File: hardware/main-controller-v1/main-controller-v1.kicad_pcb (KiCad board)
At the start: 2 copper layers, 162.7 x 112.7 mm, 62 parts, among them J1 B6B-PH-K-S, J2 Screw_Terminal_01x02, J3 Screw_Terminal_01x02, J4 Screw_Terminal_01x02, J6 Screw_Terminal_01x14, K1 G3MB-202P, K10 G3MB-202P, K11 G3MB-202P, K12 G3MB-202P, K2 G3MB-202P, K3 G3MB-202P, K4 G3MB-202P, K5 G3MB-202P, K6 G3MB-202P, K7 G3MB-202P, K8 G3MB-202P, K9 G3MB-202P, SW1 SW_Push, SW2 SW_Push, U1 ESP32-S3-WROOM-1, U2 USBLC6-2SC6, U3 LM2596S-5, U4 AP2112K-3.3

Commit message: fix(hardware): replace D2 bridge rectifier with MB10S, add bring-up jumpers, C7 footprint fix
- D2: DB107S (C5377, Extended) → MB10S (C2488, Basic); symbol+footprint
  imported via easyeda2kicad, DFM-authoritative pinout resolves the D2
  pad-swap risk that killed rev1 confidence
- Add R_JMP1-4 (0Ω 1206) on 24VAC_HOT, +VRAW, +5V, +3V3 for per-rail
  current measurement during bring-up
- C7 footprint: CP_Elec_6.3x5.4 → CP_Elec_5x5.8 (matches purchased part)
- Regenerate production/ gerbers, BOM, and CPL to match
- Track Azul.kicad_sym + Azul.pretty/MBS_* + Azul.3dshapes/ + sym-lib-table
  so the schematic resolves on a fresh clone
- Save datasheets for rev2 triac stage (MOC3062M, BT137-600E) and the
  G3MB-202P EOL catalog from Yuke Chip
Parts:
- added R_JMP1: 0, Resistor_SMD:R_1206_3216Metric, F.Cu at (106.5, 89.5)
- added R_JMP2: 0, Resistor_SMD:R_1206_3216Metric, F.Cu at (120.5, 104.0)
- added R_JMP3: 0, Resistor_SMD:R_1206_3216Metric, F.Cu at (78.5, 100.5)
- added R_JMP4: 0, Resistor_SMD:R_1206_3216Metric, F.Cu at (96.5, 72.5)
- C7: footprint Capacitor_SMD:CP_Elec_6.3x5.4 -> Capacitor_SMD:CP_Elec_5x5.8
- D2: value DB107S -> MB10S_C2488; footprint Diode_SMD:Diode_Bridge_Diotec_SO-DIL-Slim -> Azul:MBS_L4.7-W3.8-P2.40-LS7.0-TL
- moved C7 23.0 mm to (96.3, 109.0)
- moved C5 21.9 mm to (112.0, 105.5)
- moved D2 10.9 mm to (96.5, 97.5), turned to 180 degrees
- moved C6 6.85 mm to (122.5, 111.0)
- moved D1 1.00 mm to (103.5, 108.4)
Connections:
- C10 pad 1: +3V3 -> Net-(U4-VOUT)
- C6 pad 1: /+VRAW -> Net-(U3-VIN)
- C7 pad 1: +5V -> Net-(U3-FB)
- C9 pad 2: +3V3 -> Net-(U4-VOUT)
- D2 pad 1: 24VAC_HOT -> /+VRAW
- D2 pad 4: /+VRAW -> 24VAC_HOT
- F1 pad 2: Net-(J2-Pin_1) -> Net-(F1-Pad2)
- J1 pad 2: GND -> /USB_D-_RAW
- J1 pad 4: /USB_D-_RAW -> Net-(J1-Pin_4)
- J1 pad 6: Net-(J1-Pin_6) -> GND
- L1 pad 2: +5V -> Net-(U3-FB)
- R3 pad 1: Net-(J1-Pin_5) -> Net-(J1-Pin_4)
- R4 pad 1: Net-(J1-Pin_6) -> Net-(J1-Pin_5)
- U3 pad 1: /+VRAW -> Net-(U3-VIN)
- U3 pad 4: +5V -> Net-(U3-FB)
- U4 pad 5: +3V3 -> Net-(U4-VOUT)
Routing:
- net +5V: track 221.0 -> 163.9 mm, vias 4 -> 2
- net Net-(U3-FB): track 0.00 -> 47.7 mm
- net Net-(U3-VIN): track 0.00 -> 23.0 mm
- net /+VRAW: track 40.1 -> 25.6 mm
- net Net-(U4-VOUT): track 0.00 -> 11.2 mm
- net Net-(J1-Pin_6): track 9.56 -> 0.00 mm
- net Net-(J1-Pin_4): track 0.00 -> 8.97 mm
- net Net-(F1-Pad2): track 0.00 -> 5.59 mm
- net 24VAC_HOT: track 190.1 -> 185.9 mm
- net /USB_D-_RAW: track 22.6 -> 26.4 mm
- net 24VAC_COM: track 111.6 -> 110.3 mm, vias 1 -> 0
- net Net-(J2-Pin_1): track 8.59 -> 9.49 mm
- net GND: track 0.85 -> 0.00 mm, vias 49 -> 48
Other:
- board text removed: "Bridge Rectifier"

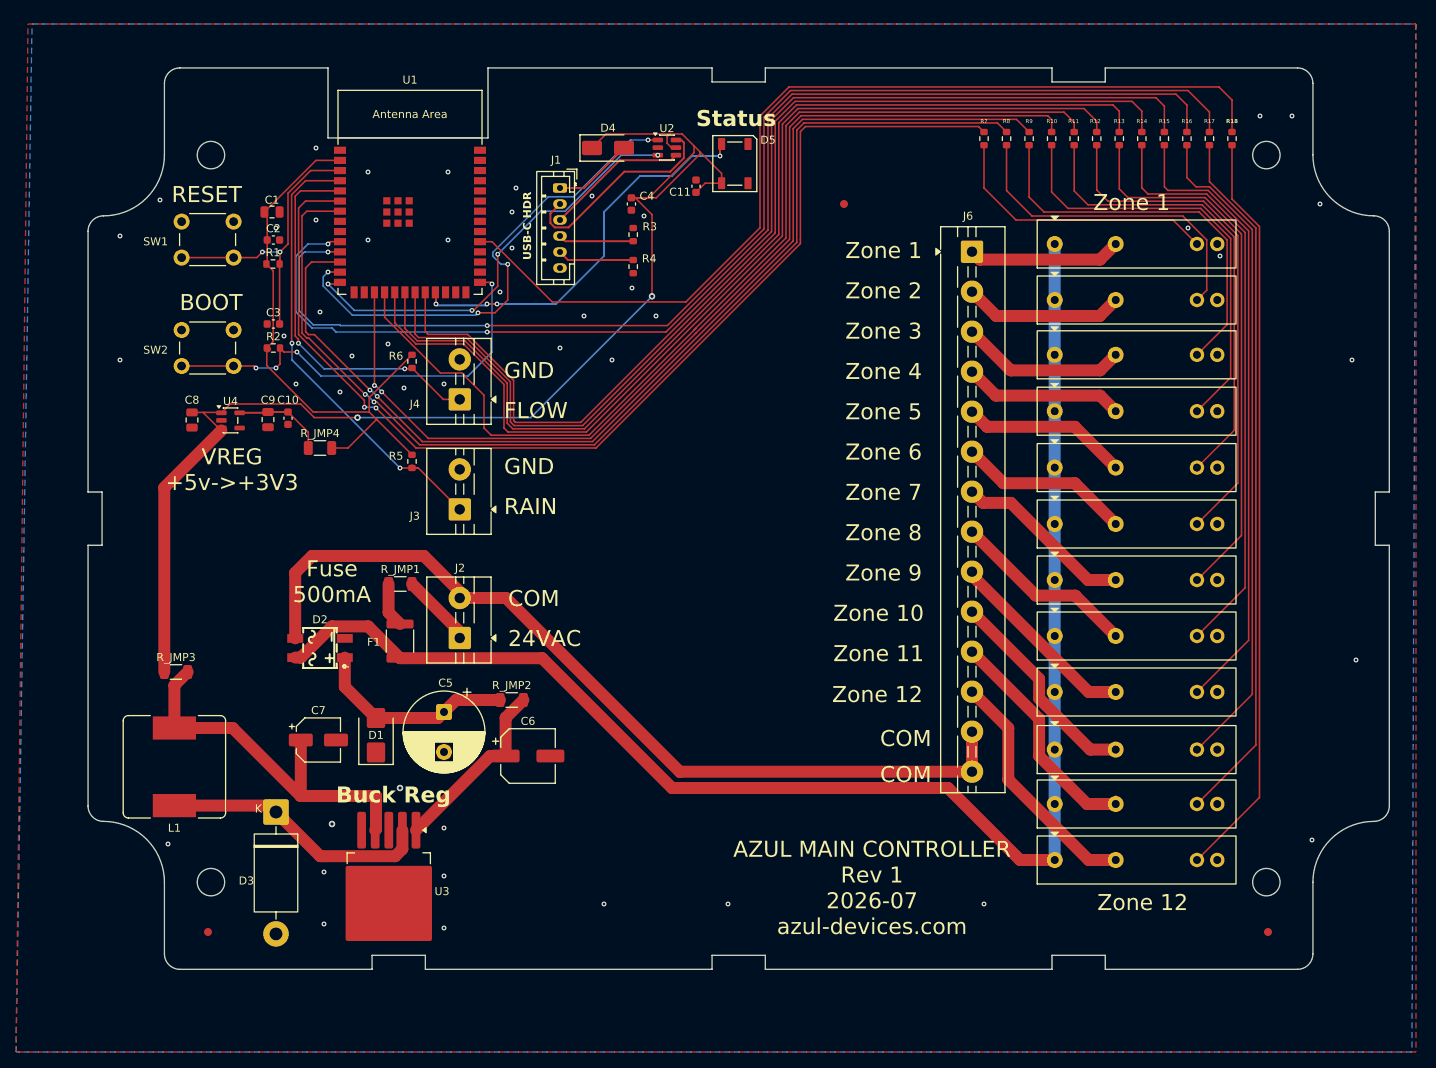
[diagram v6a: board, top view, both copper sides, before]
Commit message: feat(hardware): rev2 fab package — 12× discrete triac zone drivers
Rev2 replaces the EOL Omron G3MB-202P SSRs with a discrete triac zone-
driver topology (MOC3062M opto-isolated zero-cross trigger → BT137-600E
triac, per-zone snubber and X2 line cap). Twelve identical zone-driver
hierarchical sheets fan out from the parent under a single ribbon
header, driven active-high from the WROOM GPIOs.

Fab package uploaded to JLC 2026-08-08 as order W2026080821415396
(5 boards, Standard PCBA, UPS Express DDP, ~2026-08-18 delivery).

Design changes
- Delete K1–K12 G3MB relays; instantiate zone-driver.kicad_sch × 12
- Renumber R/C/U/Q across all 12 zone sheets (Q1–Q12 triacs,
  U5–U16 opto-drivers, C12–C23 X2 caps, R7–R42 zone stage)
- parts.yaml rev2 BOM: BT137-600E C967624, MOC3062M C8919,
  10nF X2 C105755, 39Ω 2010 snubber C2692665
- New Azul.pretty footprints + 3D models for DIP-6 opto, TO-220
  triac, and CAP-TH X2 (10mm pitch)
- Silkscreen title block "Rev 2 · 2026-08"

Fab workflow tooling
- scripts/apply_lcsc_fields.py: patches .kicad_sch LCSC fields from
  parts.yaml (BOM source of truth)
- jlc-dnp-lookup.md: fate: dnp vs smt decision matrix per part
- JLC_UPLOAD_TRACKER.md: 5-step walkthrough incorporating rev1
  lessons (J1 orientation, D2 pad-swap, CPL rotation offsets)
- Fixed DNP-flag sync bug — direct .kicad_pcb (attr) edit to strip
  stale dnp from J2/J3/J4 after fate: dnp→smt flip

Datasheets committed under docs/hardware/ for all rev2-new Extended
parts (C105755 X2, C2692665 39Ω 2010, C5188434 MX126 terminal,
C3817964, C6947975).

.gitignore: filter kicad-cli export intermediates (*.pre-*-backup,
DRC-output.rpt, update-pcb-report.txt) and the docs/azul v1 - Omega/
reference dump.
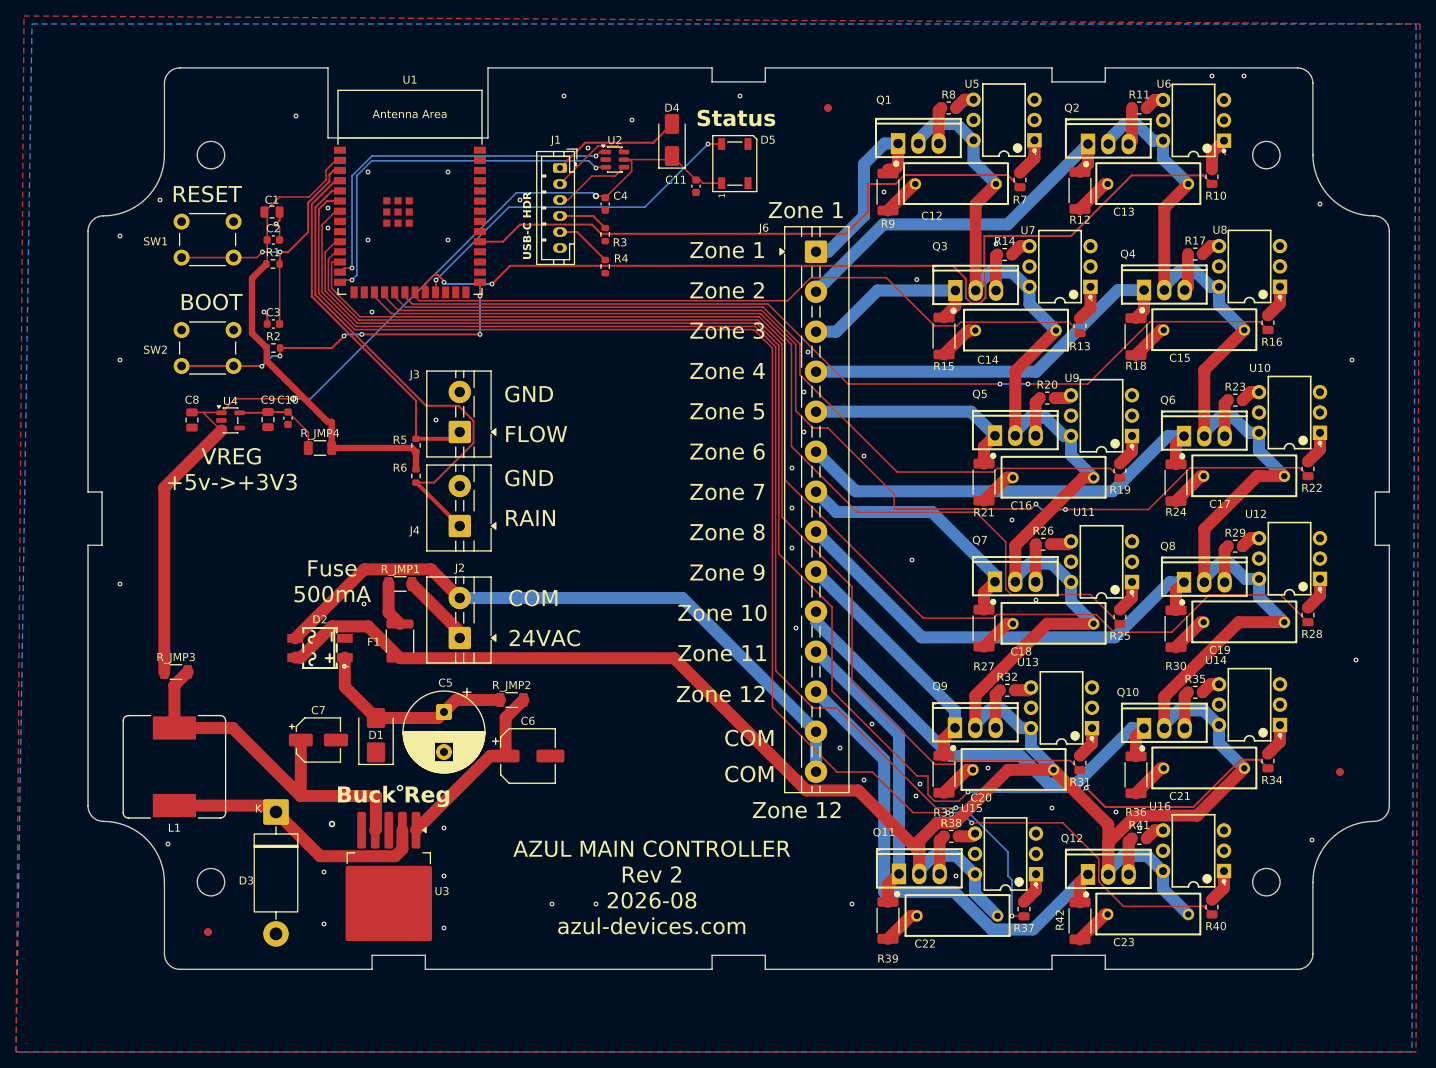
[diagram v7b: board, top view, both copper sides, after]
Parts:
- removed K1, K10, K11, K12, K2, K3, K4, K5, K6, K7, K8, K9: G3MB-202P, Azul:G3MB-202P
- added C12: 10nF, Azul:CAP-TH_L13.0-W5.0-P10.00-D1.0, F.Cu at (176.0, 39.5)
- added C13: 10nF, Azul:CAP-TH_L13.0-W5.0-P10.00-D1.0, F.Cu at (200.0, 39.5)
- added C14: 10nF, Azul:CAP-TH_L13.0-W5.0-P10.00-D1.0, F.Cu at (183.5, 57.8)
- added C15: 10nF, Azul:CAP-TH_L13.0-W5.0-P10.00-D1.0, F.Cu at (207.0, 57.8)
- added C16: 10nF, Azul:CAP-TH_L13.0-W5.0-P10.00-D1.0, F.Cu at (188.2, 76.2)
- added C17: 10nF, Azul:CAP-TH_L13.0-W5.0-P10.00-D1.0, F.Cu at (212.0, 76.0)
- added C18: 10nF, Azul:CAP-TH_L13.0-W5.0-P10.00-D1.0, F.Cu at (188.2, 94.5)
- added C19: 10nF, Azul:CAP-TH_L13.0-W5.0-P10.00-D1.0, F.Cu at (212.0, 94.3)
- added C20: 10nF, Azul:CAP-TH_L13.0-W5.0-P10.00-D1.0, F.Cu at (183.2, 112.7)
- added C21: 10nF, Azul:CAP-TH_L13.0-W5.0-P10.00-D1.0, F.Cu at (207.0, 112.5)
- added C22: 10nF, Azul:CAP-TH_L13.0-W5.0-P10.00-D1.0, F.Cu at (176.2, 131.0)
- added C23: 10nF, Azul:CAP-TH_L13.0-W5.0-P10.00-D1.0, F.Cu at (200.0, 130.8)
- added Q1: BT137-600E, Azul:TO-220-3_L10.0-W4.5-P2.54-L, F.Cu at (171.3, 34.4)
- added Q10: BT137-600E, Azul:TO-220-3_L10.0-W4.5-P2.54-L, F.Cu at (202.0, 107.5)
- added Q11: BT137-600E, Azul:TO-220-3_L10.0-W4.5-P2.54-L, F.Cu at (171.4, 125.7)
- added Q12: BT137-600E, Azul:TO-220-3_L10.0-W4.5-P2.54-L, F.Cu at (195.0, 125.8)
- added Q2: BT137-600E, Azul:TO-220-3_L10.0-W4.5-P2.54-L, F.Cu at (195.0, 34.5)
- added Q3: BT137-600E, Azul:TO-220-3_L10.0-W4.5-P2.54-L, F.Cu at (178.5, 52.8)
- added Q4: BT137-600E, Azul:TO-220-3_L10.0-W4.5-P2.54-L, F.Cu at (202.0, 52.8)
- added Q5: BT137-600E, Azul:TO-220-3_L10.0-W4.5-P2.54-L, F.Cu at (183.4, 71.0)
- added Q6: BT137-600E, Azul:TO-220-3_L10.0-W4.5-P2.54-L, F.Cu at (207.0, 71.0)
- added Q7: BT137-600E, Azul:TO-220-3_L10.0-W4.5-P2.54-L, F.Cu at (183.4, 89.2)
- added Q8: BT137-600E, Azul:TO-220-3_L10.0-W4.5-P2.54-L, F.Cu at (207.0, 89.3)
- added Q9: BT137-600E, Azul:TO-220-3_L10.0-W4.5-P2.54-L, F.Cu at (178.4, 107.5)
- added R19: 120, Resistor_SMD:R_0805_2012Metric, F.Cu at (196.5, 75.4)
- added R20: 470, Resistor_SMD:R_0805_2012Metric, F.Cu at (187.4, 66.3)
- added R21: 39, Resistor_SMD:R_2010_5025Metric, F.Cu at (179.5, 76.8)
- added R22: 120, Resistor_SMD:R_0805_2012Metric, F.Cu at (220.0, 75.1)
- added R23: 470, Resistor_SMD:R_0805_2012Metric, F.Cu at (210.9, 66.5)
- added R24: 39, Resistor_SMD:R_2010_5025Metric, F.Cu at (203.5, 76.8)
- added R25: 120, Resistor_SMD:R_0805_2012Metric, F.Cu at (196.5, 93.6)
- added R26: 470, Resistor_SMD:R_0805_2012Metric, F.Cu at (186.9, 84.5)
- added R27: 39, Resistor_SMD:R_2010_5025Metric, F.Cu at (179.5, 95.0)
- added R28: 120, Resistor_SMD:R_0805_2012Metric, F.Cu at (220.0, 93.4)
- added R29: 470, Resistor_SMD:R_0805_2012Metric, F.Cu at (210.9, 84.8)
- added R30: 39, Resistor_SMD:R_2010_5025Metric, F.Cu at (203.5, 95.1)
- added R31: 120, Resistor_SMD:R_0805_2012Metric, F.Cu at (191.5, 111.9)
- added R32: 470, Resistor_SMD:R_0805_2012Metric, F.Cu at (182.4, 102.8)
- added R33: 39, Resistor_SMD:R_2010_5025Metric, F.Cu at (174.5, 113.3)
- added R34: 120, Resistor_SMD:R_0805_2012Metric, F.Cu at (215.0, 111.6)
- added R35: 470, Resistor_SMD:R_0805_2012Metric, F.Cu at (205.9, 103.0)
- added R36: 39, Resistor_SMD:R_2010_5025Metric, F.Cu at (198.5, 113.4)
- added R37: 120, Resistor_SMD:R_0805_2012Metric, F.Cu at (184.5, 130.1)
- added R38: 470, Resistor_SMD:R_0805_2012Metric, F.Cu at (175.4, 121.0)
- added R39: 39, Resistor_SMD:R_2010_5025Metric, F.Cu at (167.5, 131.5)
- added R40: 120, Resistor_SMD:R_0805_2012Metric, F.Cu at (208.0, 129.9)
- added R41: 470, Resistor_SMD:R_0805_2012Metric, F.Cu at (198.9, 121.3)
- added R42: 39, Resistor_SMD:R_2010_5025Metric, F.Cu at (191.5, 131.6)
- added U10: MOC3062M, Azul:DIP-6_L8.5-W6.4-P2.54-LS7.6-BL, F.Cu at (217.7, 68.1)
- added U11: MOC3062M, Azul:DIP-6_L8.5-W6.4-P2.54-LS7.6-BL, F.Cu at (194.2, 86.7)
- added U12: MOC3062M, Azul:DIP-6_L8.5-W6.4-P2.54-LS7.6-BL, F.Cu at (217.7, 86.3)
- added U13: MOC3062M, Azul:DIP-6_L8.5-W6.4-P2.54-LS7.6-BL, F.Cu at (189.2, 105.0)
- added U14: MOC3062M, Azul:DIP-6_L8.5-W6.4-P2.54-LS7.6-BL, F.Cu at (212.7, 104.6)
- added U15: MOC3062M, Azul:DIP-6_L8.5-W6.4-P2.54-LS7.6-BL, F.Cu at (182.2, 123.2)
- added U16: MOC3062M, Azul:DIP-6_L8.5-W6.4-P2.54-LS7.6-BL, F.Cu at (205.7, 122.8)
- added U5: MOC3062M, Azul:DIP-6_L8.5-W6.4-P2.54-LS7.6-BL, F.Cu at (182.0, 31.5)
- added U6: MOC3062M, Azul:DIP-6_L8.5-W6.4-P2.54-LS7.6-BL, F.Cu at (205.7, 31.5)
- added U7: MOC3062M, Azul:DIP-6_L8.5-W6.4-P2.54-LS7.6-BL, F.Cu at (189.0, 49.8)
- added U8: MOC3062M, Azul:DIP-6_L8.5-W6.4-P2.54-LS7.6-BL, F.Cu at (212.7, 49.8)
- added U9: MOC3062M, Azul:DIP-6_L8.5-W6.4-P2.54-LS7.6-BL, F.Cu at (194.2, 68.5)
- R10, R13, R16, R7: value 330 -> 120; footprint Resistor_SMD:R_0603_1608Metric -> Resistor_SMD:R_0805_2012Metric
- R11, R14, R17, R8: value 330 -> 470; footprint Resistor_SMD:R_0603_1608Metric -> Resistor_SMD:R_0805_2012Metric
- R12, R15, R18, R9: value 330 -> 39; footprint Resistor_SMD:R_0603_1608Metric -> Resistor_SMD:R_2010_5025Metric
- moved R15 37.0 mm to (174.5, 58.5)
- moved R18 27.5 mm to (198.5, 58.6)
- moved R16 25.2 mm to (215.0, 56.8), turned to 90 degrees
- moved R13 23.9 mm to (191.5, 57.2), turned to 90 degrees
- moved R14 22.4 mm to (182.1, 48.3), turned to 0 degrees
- moved FID2 21.9 mm to (224.0, 113.0)
- moved R10 20.6 mm to (208.0, 38.6), turned to 90 degrees
- moved J6 19.5 mm to (158.5, 48.0)
- moved R9 18.9 mm to (167.5, 40.5)
- moved J4 15.8 mm to (114.0, 82.2)
- moved R17 14.5 mm to (205.9, 48.3), turned to 0 degrees
- moved R6 14.3 mm to (108.5, 76.0)
- moved FID3 12.2 mm to (160.0, 30.0)
- moved J3 9.67 mm to (114.0, 70.5)
- moved R11 8.99 mm to (198.9, 30.0), turned to 0 degrees
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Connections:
- R10 pad 1: /ZONE4 -> /ZONE2
- R11 pad 1: /ZONE5 -> Net-(Q2-G)
- R12 pad 1: /ZONE6 -> /Z2_OUT
- R13 pad 1: /ZONE7 -> /ZONE3
- R14 pad 1: /ZONE8 -> Net-(Q3-G)
- R15 pad 1: /ZONE9 -> /Z3_OUT
- R16 pad 1: /ZONE10 -> /ZONE4
- R17 pad 1: /ZONE11 -> Net-(Q4-G)
- R18 pad 1: /ZONE12 -> /Z4_OUT
- R8 pad 1: /ZONE2 -> Net-(Q1-G)
- R9 pad 1: /ZONE3 -> /Z1_OUT
- U1 pad 11: /ZONE11 -> /ZONE9
- U1 pad 12: /ZONE3 -> /ZONE8
- U1 pad 17: /ZONE4 -> /ZONE7
- U1 pad 18: /ZONE5 -> /ZONE6
- U1 pad 19: /ZONE6 -> /ZONE5
- U1 pad 20: /ZONE7 -> /ZONE4
- U1 pad 21: /ZONE8 -> /ZONE3
- U1 pad 22: /ZONE9 -> /ZONE2
- U1 pad 31: /ZONE12 -> /ZONE1
- U1 pad 6: /ZONE1 -> /ZONE12
- U1 pad 7: /ZONE2 -> /ZONE11
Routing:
- net 24VAC_HOT: track 185.9 -> 488.1 mm
- net Net-(C15-Pad2): track 94.0 -> 4.75 mm
- net Net-(R17-Pad2): track 87.8 -> 2.47 mm
- net Net-(U8-A): track 82.8 -> 4.22 mm
- net Net-(C14-Pad2): track 78.3 -> 5.16 mm
- net Net-(R14-Pad2): track 73.5 -> 2.62 mm
- net /ZONE1: track 139.1 -> 74.6 mm, vias 2 -> 0
- net /ZONE12: track 121.1 -> 185.4 mm, vias 0 -> 2
- net Net-(U7-A): track 68.6 -> 4.50 mm
- net Net-(C13-Pad2): track 63.8 -> 4.75 mm
- net Net-(R11-Pad2): track 58.9 -> 2.47 mm
- net Net-(U6-A): track 54.0 -> 4.22 mm
- net /ZONE3: track 134.3 -> 88.3 mm, vias 2 -> 0
- net Net-(C12-Pad2): track 49.4 -> 4.79 mm
- net +5V: track 163.9 -> 120.7 mm
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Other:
- board text added: "AZUL MAIN CONTROLLER Rev 2 2026-08 azul-devices.com"
- board text removed: "AZUL MAIN CONTROLLER Rev 1 2026-07 azul-devices.com"
